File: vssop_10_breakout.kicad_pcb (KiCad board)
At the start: 2 copper layers, 10.2 x 12.7 mm, 3 parts, among them J1 CONN_01X05, J2 CONN_01X05, U1 VSSOP-10

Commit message: Fixup silkscreen layers.
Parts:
- renumbered U1 to VSSOP
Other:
- board text added: "1"
- board text added: "10"
- board text added: "5"
- board text added: "6"
- board text added: "rpwoodbu v1"
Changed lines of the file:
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@@
     (area 138.354999 90.094999 148.665001 102.945001)
     (thickness 1.6)
-    (drawings 4)
+    (drawings 9)
     (tracks 60)
     (zones 0)
@@
     (descr "Through hole straight pin header, 1x05, 2.54mm pitch, single row")
     (tags "Through hole pin header THT 1x05 2.54mm single row")
-    (fp_text reference J1 (at 0 2.33 180) (layer B.SilkS)
+    (fp_text reference J1 (at 0 2.33 180) (layer B.SilkS) hide
       (effects (font (size 1 1) (thickness 0.15)) (justify mirror))
     )
@@
     (descr "Through hole straight pin header, 1x05, 2.54mm pitch, single row")
     (tags "Through hole pin header THT 1x05 2.54mm single row")
-    (fp_text reference J2 (at 0 2.33 180) (layer B.SilkS)
+    (fp_text reference J2 (at 0 2.33 180) (layer B.SilkS) hide
       (effects (font (size 1 1) (thickness 0.15)) (justify mirror))
     )
@@
     (tags "SSOP 0.5")
     (attr smd)
-    (fp_text reference U1 (at 0 -2.55 90) (layer F.SilkS)
-      (effects (font (size 1 1) (thickness 0.15)))
+    (fp_text reference VSSOP (at 3.81 0 180) (layer F.SilkS)
+      (effects (font (size 0.75 0.75) (thickness 0.1875)))
     )
     (fp_text value VSSOP-10 (at 0 2.55 90) (layer F.Fab)
@@
     )
   )
+  (gr_text 1 (at 140.97 91.44) (layer F.SilkS)
+    (effects (font (size 1 1) (thickness 0.25)) (justify left))
+  )
+  (gr_text 10 (at 146.05 91.44) (layer F.SilkS)
+    (effects (font (size 1 1) (thickness 0.25)) (justify right))
+  )
+  (gr_text 6 (at 146.05 101.6) (layer F.SilkS)
+    (effects (font (size 1 1) (thickness 0.25)) (justify right))
+  )
+  (gr_text 5 (at 140.97 101.6) (layer F.SilkS)
+    (effects (font (size 1 1) (thickness 0.25)) (justify left))
+  )
+  (gr_text "rpwoodbu\nv1" (at 143.51 101.6) (layer B.SilkS)
+    (effects (font (size 0.5 0.5) (thickness 0.125)) (justify mirror))
+  )
   (gr_line (start 138.43 102.87) (end 138.43 90.17) (layer Edge.Cuts) (width 0.15))

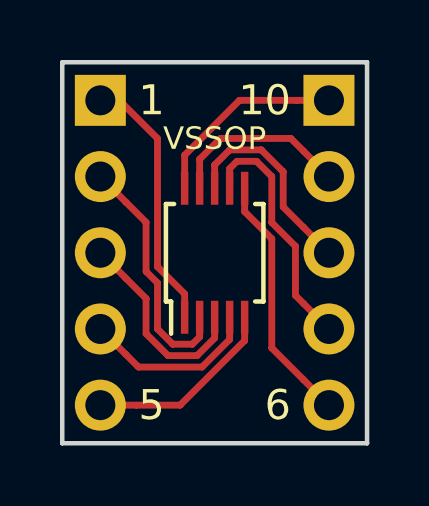
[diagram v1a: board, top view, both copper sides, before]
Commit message: Redo layout with new footprint.
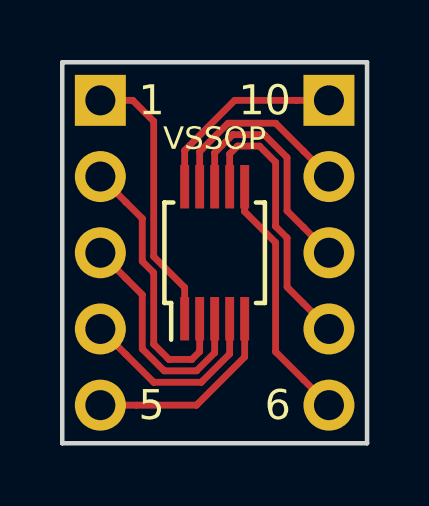
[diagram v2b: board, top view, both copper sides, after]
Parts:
- removed VSSOP: VSSOP-10, Housings_SSOP:TSSOP-10_3x3mm_Pitch0.5mm
- added U1: VSSOP, VSSOP:VSSOP-10_3x3mm_Pitch0.5mm, F.Cu at (143.5, 96.5)
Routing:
- net Net-(J1-Pad2): track 8.24 -> 9.27 mm
- net Net-(J1-Pad3): track 6.85 -> 7.88 mm
- net Net-(J2-Pad3): track 6.90 -> 7.92 mm
- net Net-(J2-Pad4): track 8.24 -> 9.25 mm
- net Net-(J1-Pad4): track 5.96 -> 6.66 mm
- net Net-(J2-Pad2): track 6.09 -> 6.66 mm

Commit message: Make back silkscreen more interesting.
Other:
- board text added: "github.com/ rpwoodbu/ vssop_10_breakout"
- board text added: "rpwoodbu jbebel v1"
- board text removed: "rpwoodbu v1"
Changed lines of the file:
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@@
     (area 138.354999 90.094999 148.665001 102.945001)
     (thickness 1.6)
-    (drawings 9)
+    (drawings 10)
     (tracks 60)
     (zones 0)
@@
     )
   )
+  (gr_text "github.com/\nrpwoodbu/\nvssop_10_breakout" (at 143.51 102.616 270) (layer B.SilkS)
+    (effects (font (size 0.5 0.5) (thickness 0.125)) (justify left mirror))
+  )
   (gr_text 1 (at 140.97 91.44) (layer F.SilkS)
     (effects (font (size 1 1) (thickness 0.25)) (justify left))
@@
     (effects (font (size 1 1) (thickness 0.25)) (justify left))
   )
-  (gr_text "rpwoodbu\nv1" (at 143.51 101.6) (layer B.SilkS)
-    (effects (font (size 0.5 0.5) (thickness 0.125)) (justify mirror))
+  (gr_text "rpwoodbu\njbebel\nv1" (at 143.51 90.424 270) (layer B.SilkS)
+    (effects (font (size 0.5 0.5) (thickness 0.125)) (justify right mirror))
   )
   (gr_line (start 138.43 102.87) (end 138.43 90.17) (layer Edge.Cuts) (width 0.15))
